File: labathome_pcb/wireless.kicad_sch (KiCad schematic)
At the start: 10 parts, among them J14 LoRa Antenna, U16 MODULE_STEPDOWN, U17 RFM95W-868S2

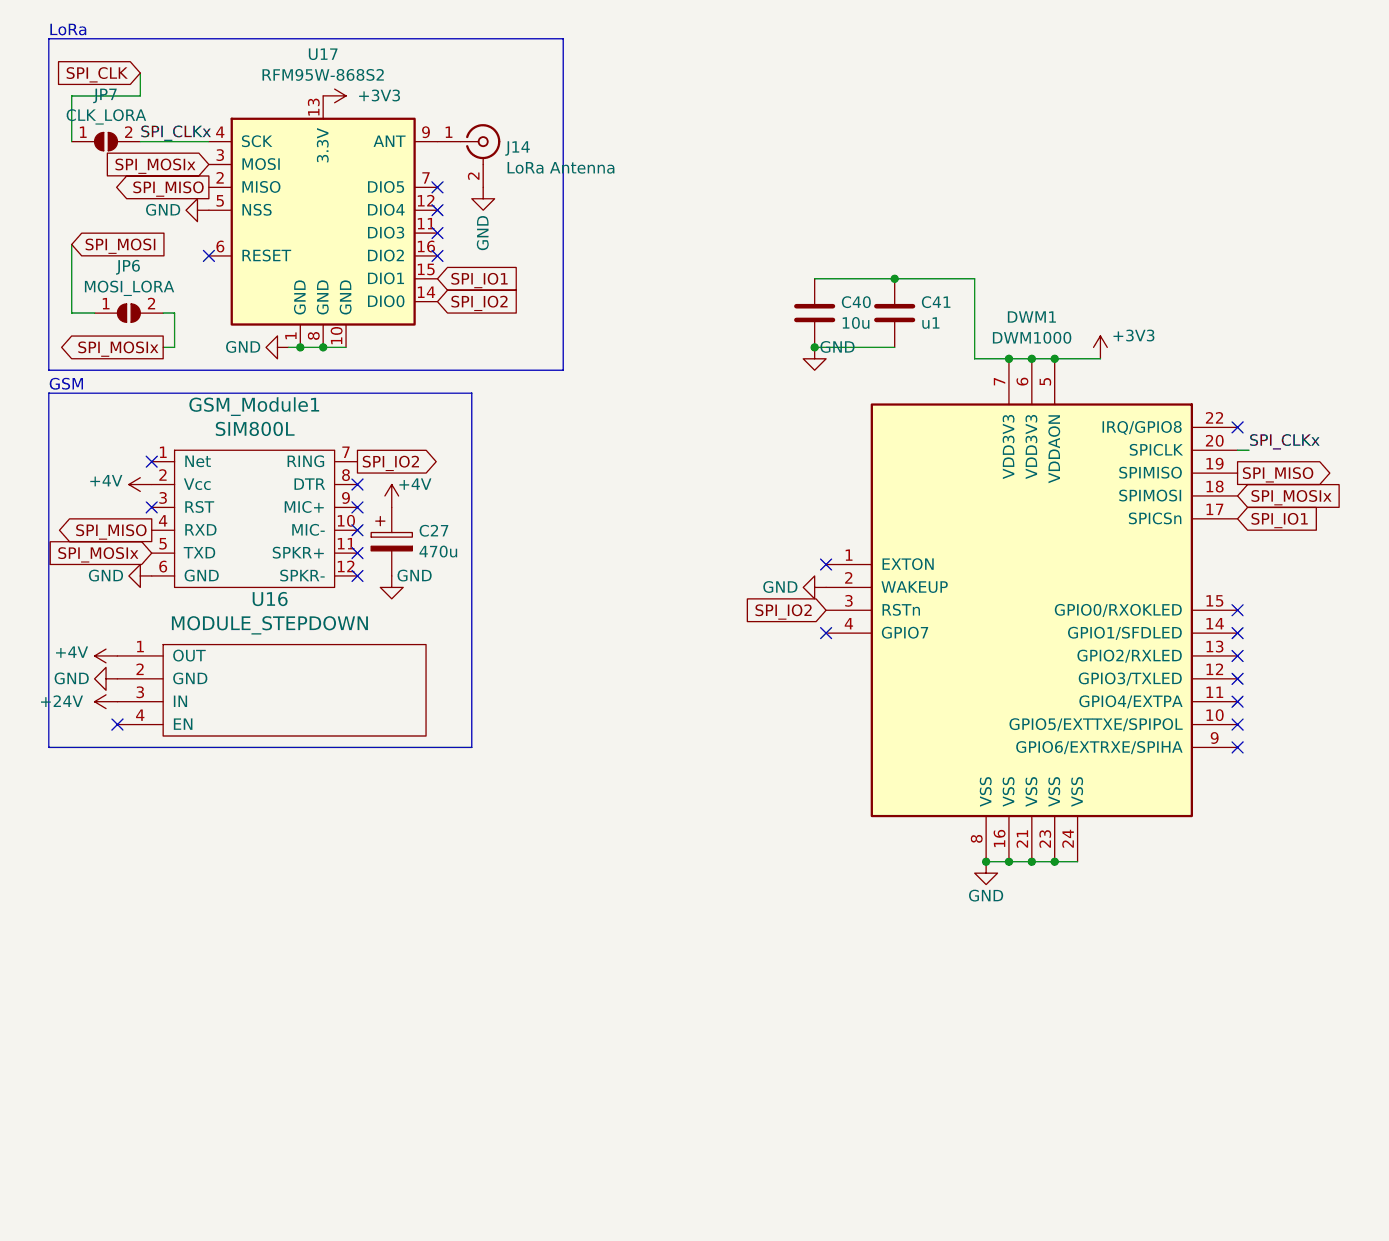
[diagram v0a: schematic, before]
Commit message: Updated PCB: nRF24l01, SIM7080, LoRa module
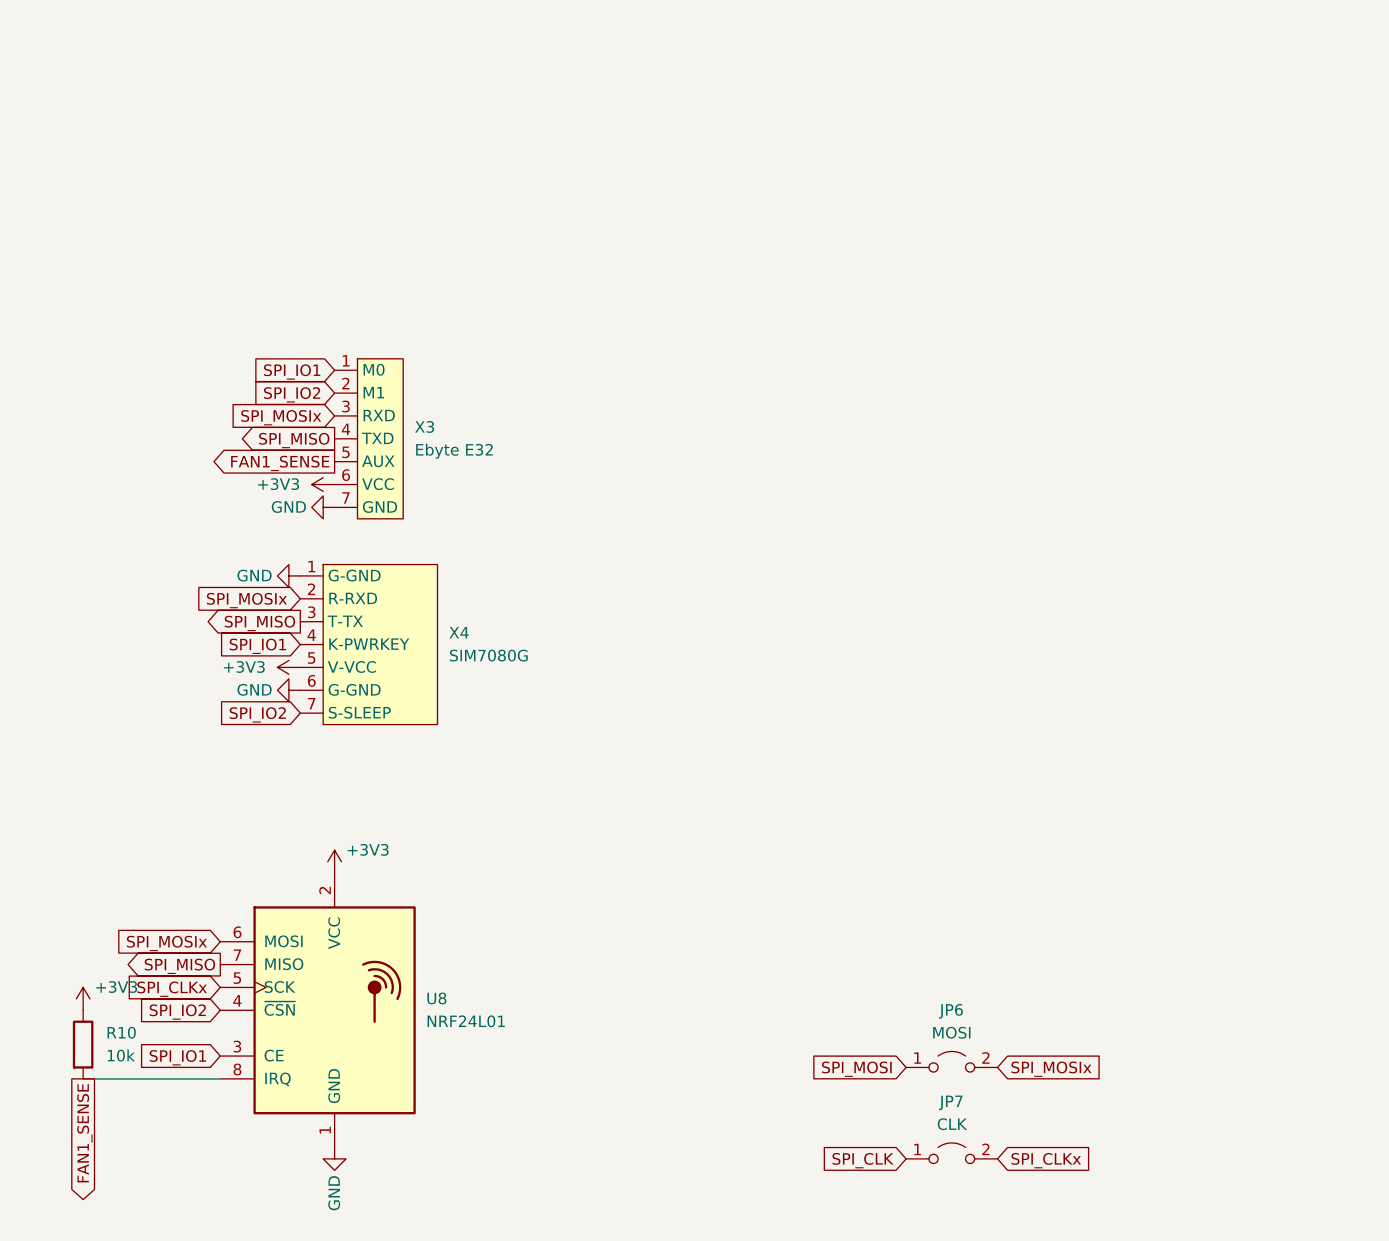
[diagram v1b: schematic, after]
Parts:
- removed C27: 470u, Capacitor_THT:CP_Radial_D8.0mm_P3.50mm, symbol Device:CP
- removed C40: 10u, Capacitor_SMD:C_0805_2012Metric_Pad1.18x1.45mm_HandSolder, symbol Device:C
- removed C41: u1, Capacitor_SMD:C_0805_2012Metric_Pad1.18x1.45mm_HandSolder, symbol Device:C
- removed DWM1: DWM1000, RF_Module:DWM1000, symbol RF_Module:DWM1000
- removed GSM_Module1: SIM800L, liebler_MODULES:SIM800L, symbol liebler_MODULES:SIM800L
- removed J14: LoRa Antenna, Connector_Coaxial:SMA_Samtec_SMA-J-P-X-ST-EM1_EdgeMount, symbol Connector:Conn_Coaxial
- removed JP6: MOSI_LORA, Jumper:SolderJumper-2_P1.3mm_Open_RoundedPad1.0x1.5mm, symbol Jumper:SolderJumper_2_Open
- removed JP7: CLK_LORA, Jumper:SolderJumper-2_P1.3mm_Open_RoundedPad1.0x1.5mm, symbol Jumper:SolderJumper_2_Open
- removed U16: MODULE_STEPDOWN, liebler_MODULES:MODULE_STEPDOWN, symbol sensact:MODULE_STEPDOWN
- removed U17: RFM95W-868S2, RF_Module:HOPERF_RFM9XW_SMD, symbol RF_Module:RFM95W-868S2
- added JP6: MOSI, Jumper:SolderJumper-2_P1.3mm_Open_RoundedPad1.0x1.5mm, symbol Jumper:Jumper_2_Open
- added JP7: CLK, Jumper:SolderJumper-2_P1.3mm_Open_RoundedPad1.0x1.5mm, symbol Jumper:Jumper_2_Open
- added R10: 10k, Resistor_SMD:R_0402_1005Metric, symbol Device:R
- added U8: NRF24L01, RF_Module:nRF24L01_Breakout, symbol RF:NRF24L01_Breakout
- added X3: Ebyte E32, liebler_MODULES:Ebyte-E32-900T20D, symbol liebler_MODULES:Ebyte-E32-900T20D
- added X4: SIM7080G, liebler_MODULES:SIM7080G_AND_MODULE, symbol liebler_MODULES:SIM7080G_AND_MODULE
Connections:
- net +3V3: now also R10.1, U8.2 (VCC), X3.6 (VCC), X4.5 (V-VCC)
- net GND: now also U8.1 (GND), X3.7 (GND), X4.1 (G-GND), X4.6 (G-GND)
- net SPI_CLK: now also JP7.1 (A)
- net SPI_CLKx: now also JP7.2 (B), U8.5 (SCK)
- net SPI_IO1: now also U8.3 (CE), X3.1 (M0), X4.4 (K-PWRKEY)
- net SPI_IO2: now also U8.4 (~{CSN}), X3.2 (M1), X4.7 (S-SLEEP)
- net SPI_MISO: now also U8.7 (MISO), X3.4 (TXD), X4.3 (T-TX)
- net SPI_MOSI: now also JP6.1 (A)
- net SPI_MOSIx: now also JP6.2 (B), U8.6 (MOSI), X3.3 (RXD), X4.2 (R-RXD)
- new net FAN1_SENSE: R10.2, U8.8 (IRQ), X3.5 (AUX)
- no-connect marks 23 -> 0
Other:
- note removed: "GSM"
- note removed: "LoRa"
